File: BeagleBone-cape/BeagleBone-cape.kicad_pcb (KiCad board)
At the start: 4 copper layers, 86.4 x 54.6 mm, 97 parts, among them IC1 A6983C50QTR, IC2 TCAN3413DDFR, IC3 BMP390, J1 Servo 0, J10 MotorR, J11 CAN, J12 24V, J13 MAVLink, J2 Servo 1, J3 Servo 2, J4 Servo 3, J5 LEDL, J6 LEDR, J8 Air Speed Sensor, J9 MotorL, P8 BeagleBone_Black_Header, P9 BeagleBone_Black_Header, Q1 DMP3013SFV, Q2 Q_NMOS_GSD, U10 IIS2MDC, U3 DS1307ZN+, U6 LTC4412ES6, U9 LSM6DSV16X, Y1 32.768kHz

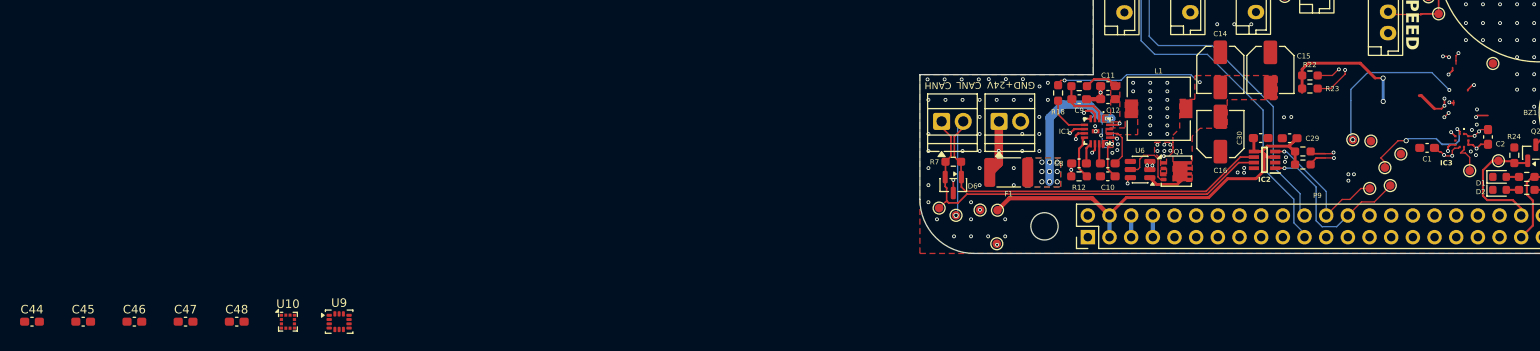
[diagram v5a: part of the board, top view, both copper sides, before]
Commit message: Cape: finish IMU/baro schematic, PCB sync and cleanup
Schematic:
- remove cape EEPROM U1, SW1, TP1 (#4)
- PGOOD to P8.12 via 10k pull-up R27 (#10)
- PWR_FLAGs on root, VBUS renamed SYS_5V, GPIO2/3 renamed UART_RX/TX (#6, #12, #33)
- VBIAS of A6983 to BUCK_OUT (#34)
- BMP390 symbol moved to Cape_lib, MPN fixed BMP388 -> BMP390 (#13)
- LSM6DSV16X/IIS2MDC: add C49 10 uF decoupling, fix C48 value/MPN (datasheet audit)

PCB:
- sync from schematic, place U9, U10, C44-C49, R27
- remove stray IMU-area +3V3/IMU_INT1 copper, old +3V3 In2 pour, dangling copper (#17, #18)
- design rules: outer track 0.10 mm, edge clearance 0.3 mm, zone clearance 0.2 mm (#37)

Routing is not done: 46 unconnected pads remain for manual routing.
DRC: 1 courtyard overlap (R27/R18), 7 pre-existing lib_footprint_mismatch warnings.
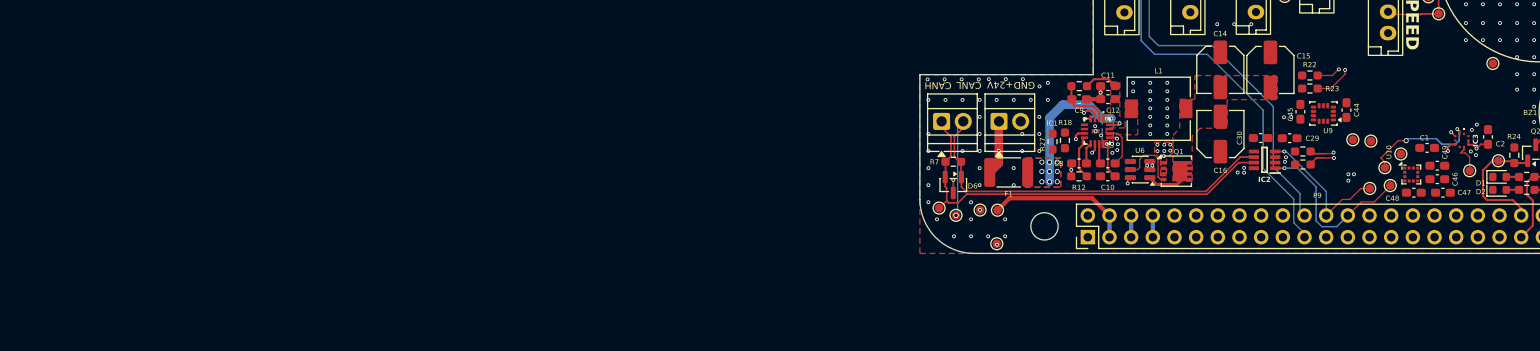
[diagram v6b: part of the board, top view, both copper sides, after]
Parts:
- added C49: 10u, Capacitor_SMD:C_0603_1608Metric_Pad1.08x0.95mm_HandSolder, F.Cu at (160.7, 89.7)
- added R27: 10k, Resistor_SMD:R_0603_1608Metric_Pad0.98x0.95mm_HandSolder, F.Cu at (115.5, 86.9)
- moved C44 156.1 mm to (150.0, 83.2), turned to -90 degrees
- moved C46 153.6 mm to (160.7, 91.3)
- moved C47 148.2 mm to (161.3, 92.9)
- moved C45 144.8 mm to (144.6, 83.4), turned to -90 degrees
- moved C48 138.8 mm to (157.9, 92.9)
- moved U10 132.8 mm to (157.6, 90.8)
- moved U9 117.9 mm to (147.3, 83.6), turned to 180 degrees
- moved R18 5.62 mm to (117.0, 86.8), turned to -90 degrees
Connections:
- net /GPIO2 renamed /UART_RX
- net /GPIO3 renamed /UART_TX
- net VBUS renamed /SYS_5V
- IC1 pad 5: /Power/PGOOD -> /PGOOD
- IC1 pad 6: GND -> /Power/BUCK_OUT
- P8 pad 12: unconnected-(P8-Pin_12-Pad12) -> /PGOOD
- R18 pad 1: /Power/PGOOD -> /PGOOD
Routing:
- net +3V3: track 80.9 -> 17.2 mm, vias 12 -> 0
- net /IMU_INT1: track 19.3 -> 0.00 mm, vias 2 -> 0
- net /Power/BUCK_OUT: track 22.8 -> 5.24 mm, vias 2 -> 0
- net GND: track 26.6 -> 18.7 mm, vias 302 -> 295
- net /Power/PGOOD: track 5.22 -> 0.00 mm
- removed copper zone on In2.Cu, net +3V3

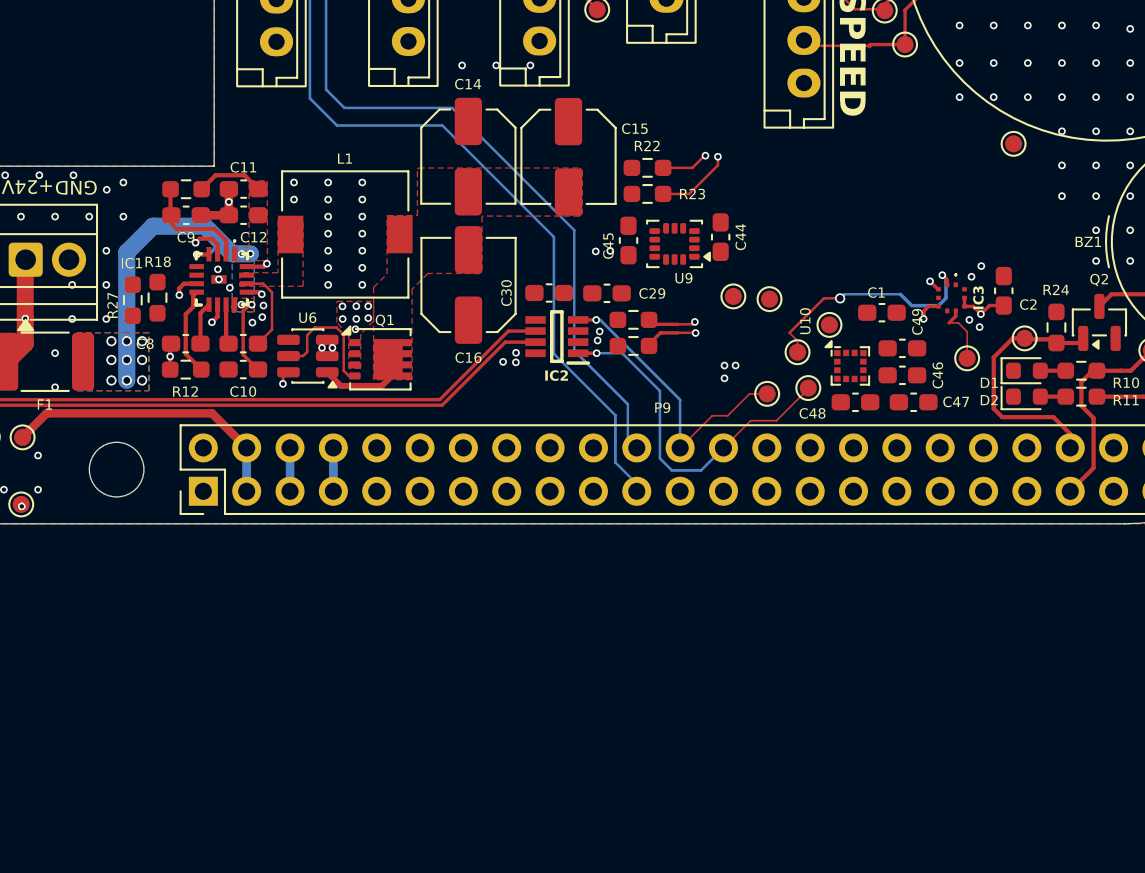
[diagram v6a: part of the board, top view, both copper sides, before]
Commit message: Cape PCB: manual layout changes saved in KiCad after 536a2f9b
Parts repositioned in KiCad (e.g. C49 at 163.42, 77.94). DRC on this state:
83 violations, 52 unconnected pads (routing still to do).
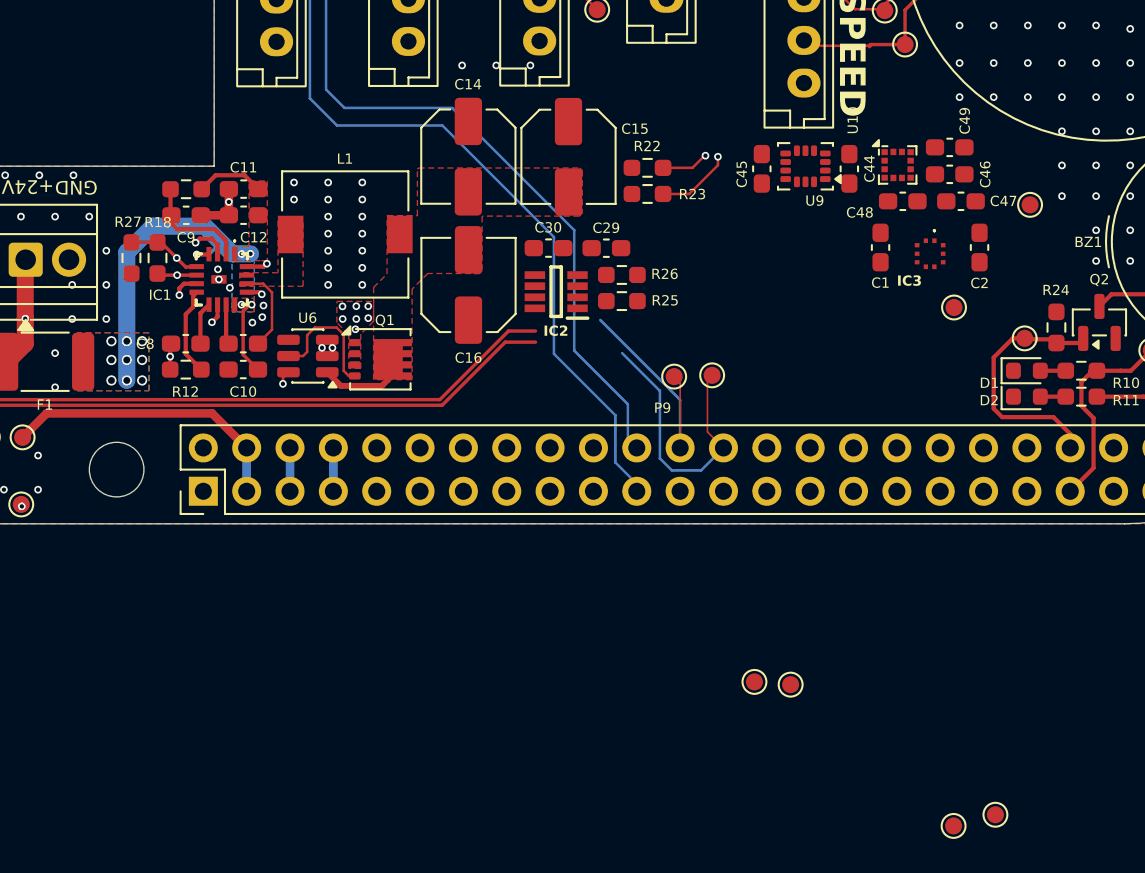
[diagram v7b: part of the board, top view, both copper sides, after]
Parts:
- moved TP20 30.3 mm to (166.1, 117.0)
- moved TP19 29.2 mm to (163.7, 117.7)
- moved TP23 22.6 mm to (152.0, 109.3)
- moved TP24 22.6 mm to (154.1, 109.4)
- moved C46 12.1 mm to (163.4, 79.5)
- moved C49 12.1 mm to (163.4, 77.9)
- moved U10 12.1 mm to (160.4, 79.0)
- moved C47 12.1 mm to (164.1, 81.1)
- moved C48 12.1 mm to (160.7, 81.1)
- moved U9 8.92 mm to (155.0, 79.0)
- moved C45 8.87 mm to (152.4, 79.2)
- moved C44 8.54 mm to (157.5, 79.2)
- moved TP30 5.68 mm to (149.5, 91.3)
- moved TP31 5.54 mm to (147.3, 91.4)
- moved C1 3.82 mm to (159.4, 83.8), turned to 90 degrees
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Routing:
- net /I2C1.SCL: track 31.7 -> 11.6 mm, vias 3 -> 0
- net /I2C1.SDA: track 15.5 -> 9.42 mm, vias 1 -> 0
- net GND: track 18.7 -> 13.2 mm, vias 295 -> 275
- net /PGOOD: track 0.03 -> 4.46 mm, vias 0 -> 1
- net /FDCAN_TX: track 20.7 -> 16.4 mm, vias 1 -> 0
- net /BARO_INT: track 3.71 -> 0.00 mm
- net /FDCAN_RX: track 17.1 -> 13.8 mm, vias 1 -> 0
- net /Power/BUCK_OUT: track 5.24 -> 7.54 mm, vias 0 -> 1

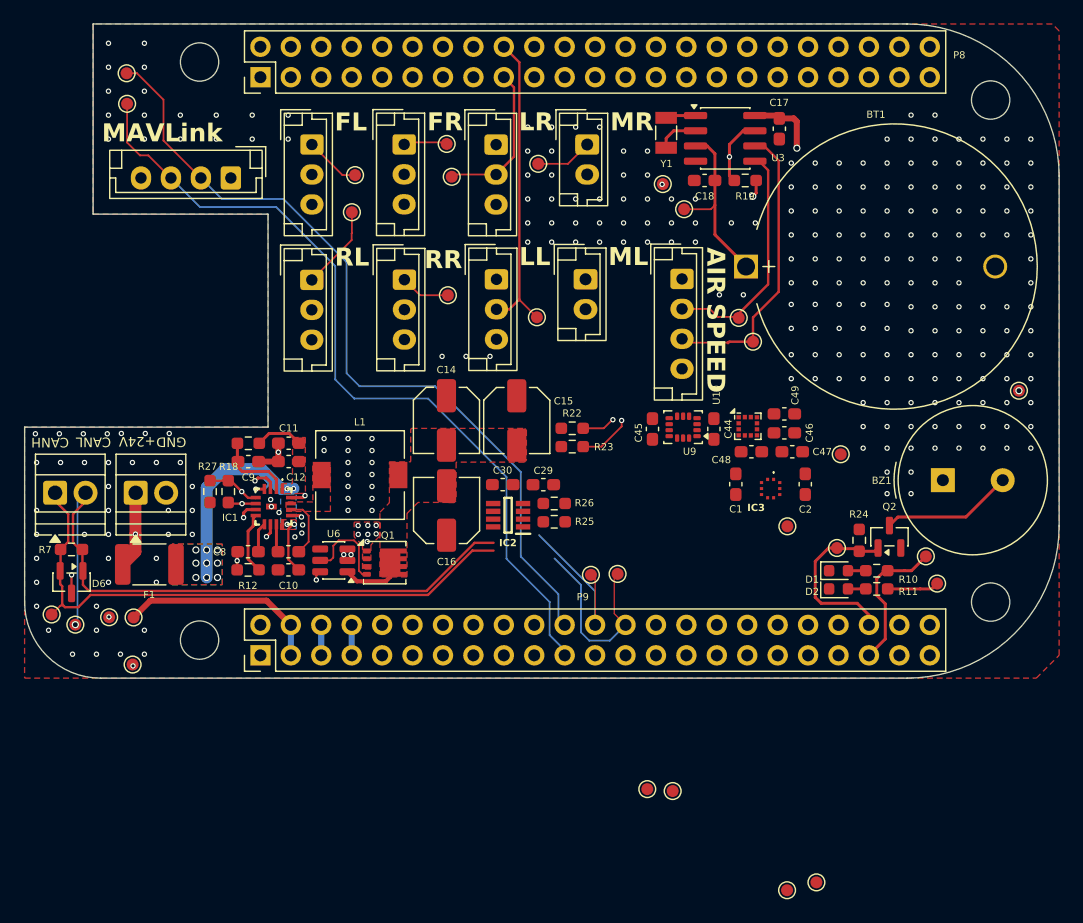
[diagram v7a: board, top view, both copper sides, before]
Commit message: Cape: add baro and IMU/mag schematic sheets, sync root/PCB/project files
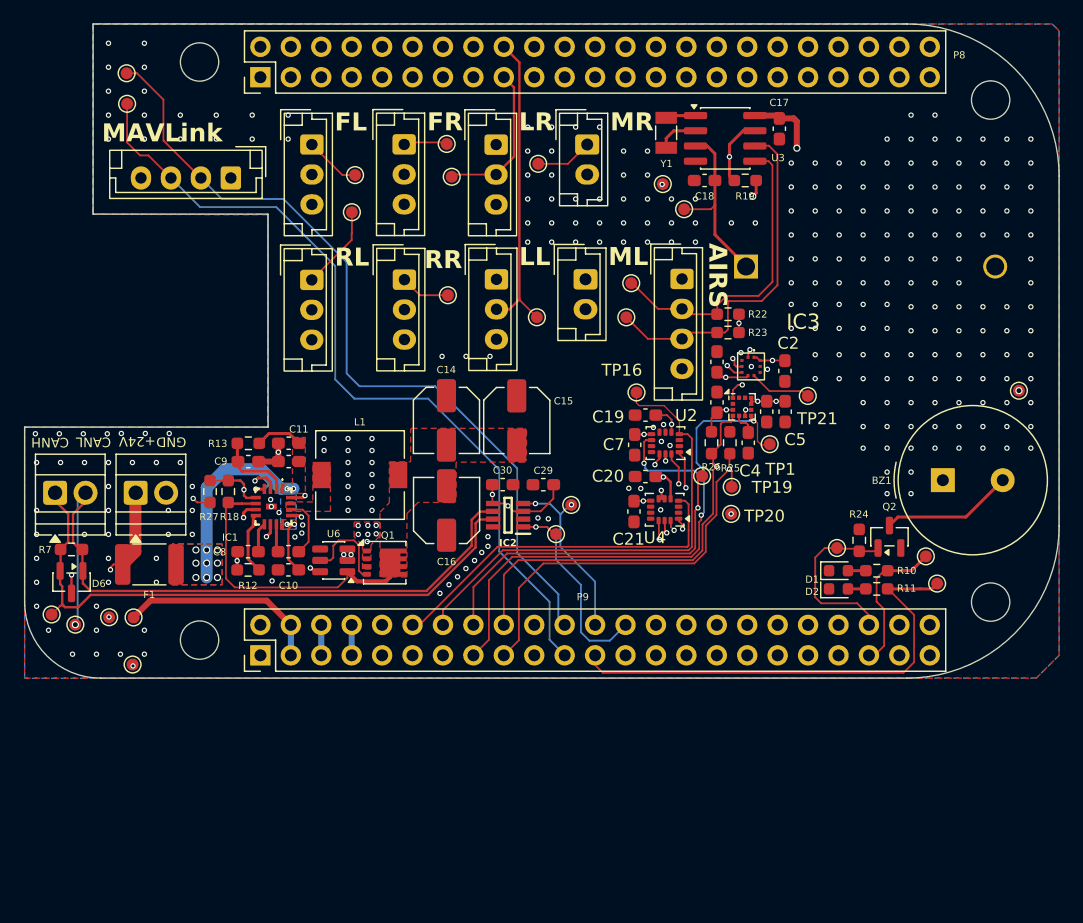
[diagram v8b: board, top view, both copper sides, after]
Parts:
- removed C44, C45, C46, C47: 100n, Capacitor_SMD:C_0603_1608Metric_Pad1.08x0.95mm_HandSolder
- removed C48: 220n, Capacitor_SMD:C_0603_1608Metric_Pad1.08x0.95mm_HandSolder
- removed C49: 10u, Capacitor_SMD:C_0603_1608Metric_Pad1.08x0.95mm_HandSolder
- removed TP23, TP24: TestPoint, TestPoint:TestPoint_Pad_D1.0mm
- removed U10: IIS2MDC, Package_LGA:LGA-12_2x2mm_P0.5mm
- removed U9: LSM6DSV16X, Package_LGA:LGA-14_3x2.5mm_P0.5mm_LayoutBorder3x4y
- added C19: 100n, Capacitor_SMD:C_0603_1608Metric_Pad1.08x0.95mm_HandSolder, F.Cu at (151.8, 78.0)
- added C20: 100n, Capacitor_SMD:C_0603_1608Metric_Pad1.08x0.95mm_HandSolder, F.Cu at (151.8, 83.2)
- added C21: 100n, Capacitor_SMD:C_0603_1608Metric_Pad1.08x0.95mm_HandSolder, F.Cu at (150.9, 86.1)
- added C3: 100n, Capacitor_SMD:C_0603_1608Metric_Pad1.08x0.95mm_HandSolder, F.Cu at (161.9, 77.8)
- added C4: 220n, Capacitor_SMD:C_0603_1608Metric_Pad1.08x0.95mm_HandSolder, F.Cu at (160.4, 80.4)
- added C5: 100n, Capacitor_SMD:C_0603_1608Metric_Pad1.08x0.95mm_HandSolder, F.Cu at (163.5, 77.8)
- added C6: 10u, Capacitor_SMD:C_0603_1608Metric_Pad1.08x0.95mm_HandSolder, F.Cu at (157.8, 77.0)
- added C7: 100n, Capacitor_SMD:C_0603_1608Metric_Pad1.08x0.95mm_HandSolder, F.Cu at (150.9, 80.5)
- added TP1: TestPoint, TestPoint:TestPoint_Pad_D1.0mm, F.Cu at (162.2, 80.5)
- added TP17: TestPoint, TestPoint:TestPoint_Pad_D1.0mm, F.Cu at (156.6, 83.1)
- added U1: IIS2MDC, Package_LGA:LGA-12_2x2mm_P0.5mm, F.Cu at (159.9, 77.4)
- added U2: LSM6DSV16X, Package_LGA:LGA-14_3x2.5mm_P0.5mm_LayoutBorder3x4y, F.Cu at (153.5, 80.4)
- added U4: LSM6DSV16X, Package_LGA:LGA-14_3x2.5mm_P0.5mm_LayoutBorder3x4y, F.Cu at (153.4, 85.9)
- BT1: moved to B.Cu
- moved TP19 34.0 mm to (159.0, 84.0)
- moved TP20 31.6 mm to (159.0, 86.3)
- moved TP16 17.8 mm to (151.1, 76.2)
- moved R22 16.1 mm to (158.7, 69.6), turned to 180 degrees
- moved R23 16.1 mm to (158.7, 71.2), turned to 180 degrees
- moved R25 16.1 mm to (158.9, 80.3), turned to -90 degrees
- moved R26 14.1 mm to (157.3, 80.3), turned to -90 degrees
- moved TP21 11.0 mm to (165.4, 76.4)
- moved TP13 10.8 mm to (150.2, 69.9)
- moved C1 10.3 mm to (157.8, 73.6)
- moved IC3 10.3 mm to (160.6, 74.0)
- moved C2 9.60 mm to (163.5, 74.4)
- moved TP12 9.43 mm to (150.6, 67.0)
- moved TP30 6.12 mm to (144.4, 88.0)
- moved TP31 6.06 mm to (145.6, 85.5)
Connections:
- P9 pad 12: /GPIO60 -> /IMU2_INT1
- P9 pad 14: /IMU_INT1 -> /IMU_INT2
- P9 pad 16: /IMU_INT2 -> /IMU_INT1
- P9 pad 27: /GPIO125 -> /IMU2_CS
- TP16 pad 1: /MAG_DRDY -> /IMU_INT2
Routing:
- net /MAG_DRDY: track 0.00 -> 44.5 mm, vias 0 -> 2
- net /I2C1.SDA: track 9.42 -> 50.1 mm, vias 0 -> 3
- net /IMU_INT2: track 0.35 -> 40.6 mm
- net /IMU_INT1: track 0.00 -> 39.8 mm, vias 0 -> 2
- net /I2C1.SCL: track 11.6 -> 47.2 mm, vias 0 -> 3
- net /GPIO49: track 4.86 -> 40.2 mm
- net +3V3: track 17.2 -> 49.6 mm, vias 0 -> 13
- net /IMU2_INT1: track 0.00 -> 30.1 mm
- net /SPI1.SCLK: track 0.00 -> 24.2 mm, vias 0 -> 2
- net /SPI1.D0: track 0.00 -> 19.8 mm, vias 0 -> 2
- net /Power/BUCK_OUT: track 7.54 -> 26.3 mm, vias 1 -> 0
- net /SPI1.CS0: track 0.00 -> 17.9 mm, vias 0 -> 1
- net /SPI1.D1: track 0.00 -> 16.2 mm, vias 0 -> 2
- net /IMU2_CS: track 0.00 -> 12.5 mm, vias 0 -> 1
- net /BARO_INT: track 0.00 -> 5.18 mm
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- added copper zone on B.Cu, net +3V3
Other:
- board text added: "AIRS"
- board text removed: "AIR SPEED"
